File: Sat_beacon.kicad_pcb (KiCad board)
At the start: 4 copper layers, 123.9 x 79.5 mm, 126 parts, among them IC1 LMX2581ESQE_NOPB, IC2 LMX2581ESQE_NOPB, J1 Conn_01x05_Pin, J2 Conn_01x03_Pin, J4 SMA, J5 SMA, J6 Conn_01x04_Pin, Q1 BC817-40, Q2 BC817-40, Q3 BC817-40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

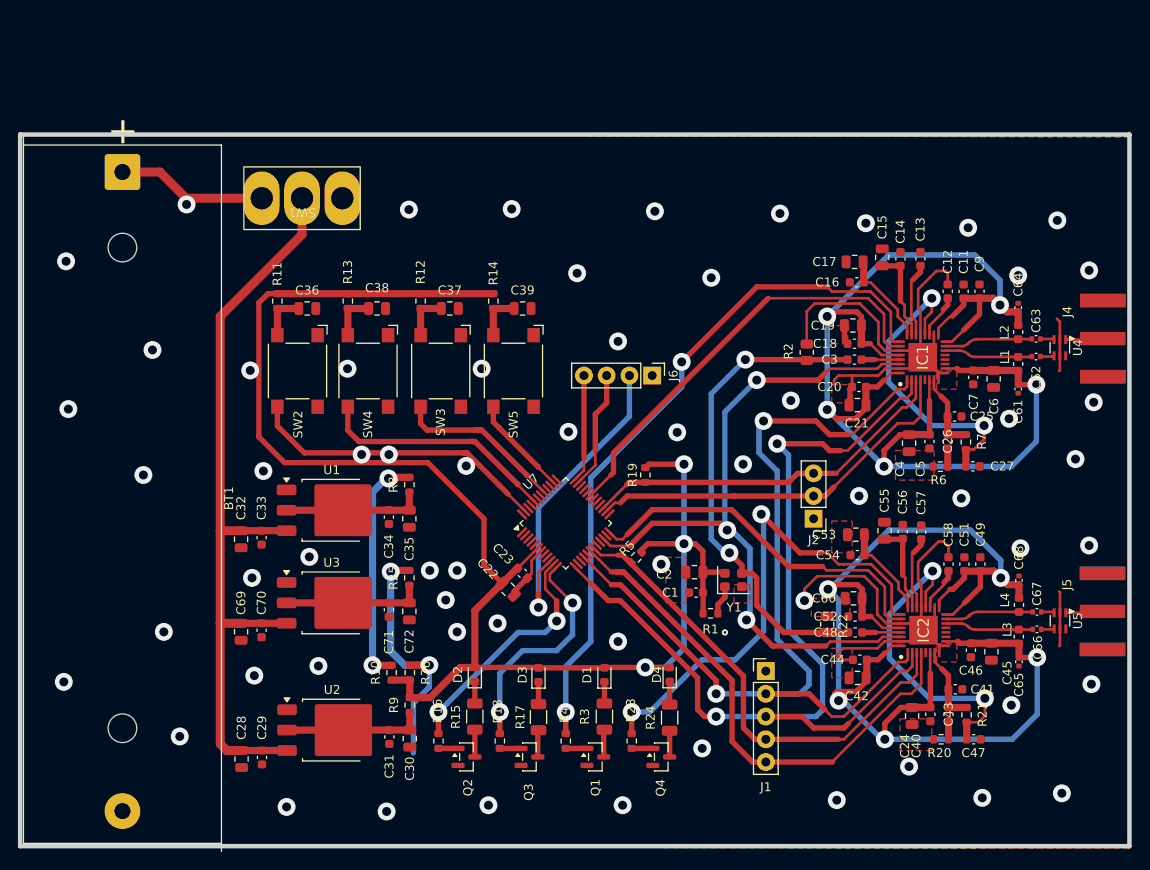
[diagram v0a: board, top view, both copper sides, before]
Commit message: PCB constrains updated for china + added vias, improved vias thanks to improved constrains
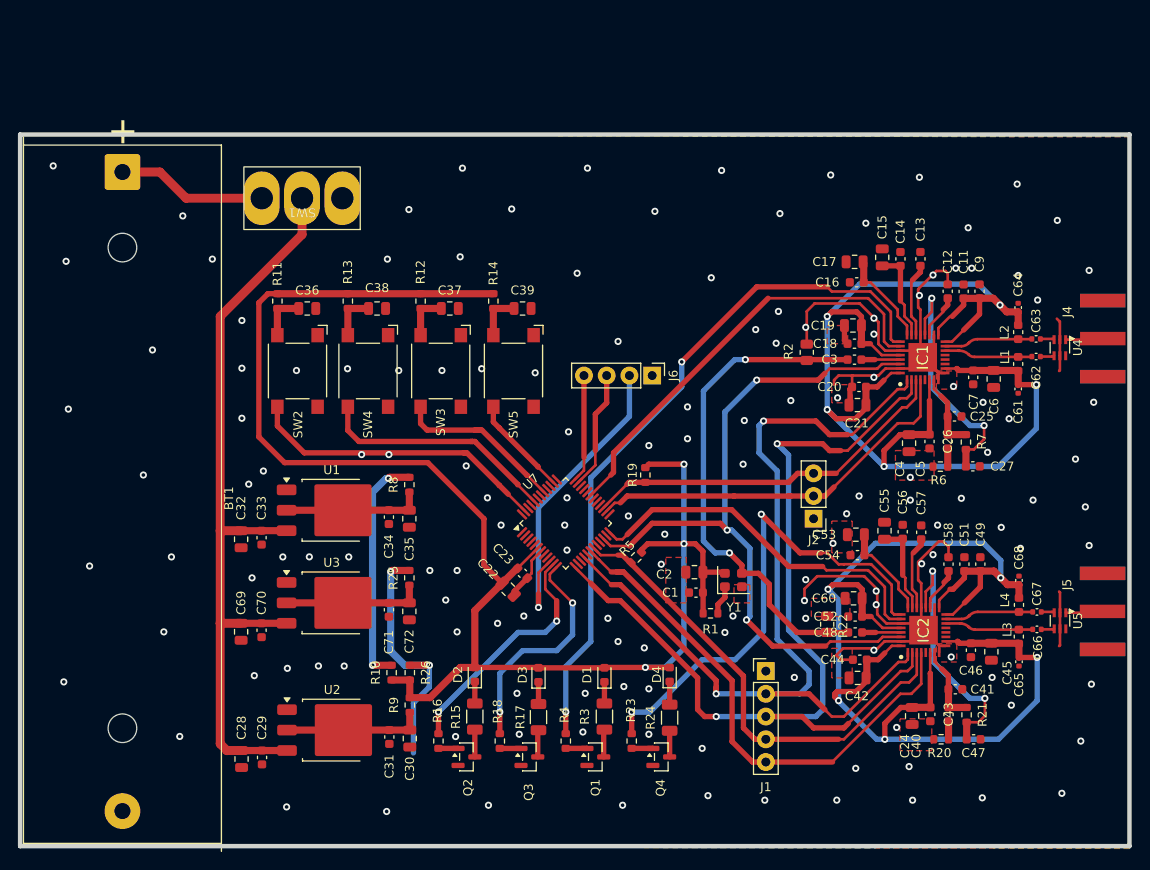
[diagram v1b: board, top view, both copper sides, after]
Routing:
- net /VTUNE_2: track 34.9 -> 28.2 mm
- net /VTUNE_1: track 34.4 -> 28.0 mm
- net VCC_PLL1: track 167.3 -> 162.1 mm, vias 9 -> 7
- net VCC_PLL2: track 169.2 -> 167.1 mm
- net /CLK_10MHZ: track 54.7 -> 56.3 mm
- net GND: vias 58 -> 143
- net /PLL_BTN_1: vias 0 -> 2

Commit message: PCB done and ordered
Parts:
- moved BT1 35.7 mm to (92.2, 50.0), turned to 0 degrees
- moved C69 6.44 mm to (76.3, 108.7), turned to 180 degrees
- moved C32 6.42 mm to (76.3, 98.3), turned to 180 degrees
- moved C28 6.39 mm to (76.3, 122.9), turned to 180 degrees
- moved SW1 4.21 mm to (78.6, 54.6), turned to 90 degrees
- moved J4 1.46 mm to (164.9, 74.4)
- moved J5 1.31 mm to (165.1, 104.9)
- moved C61 1.21 mm to (155.7, 79.9)
- moved C62 1.21 mm to (157.7, 76.3)
- moved C63 1.21 mm to (157.7, 74.3)
- moved L1 1.21 mm to (155.7, 77.1)
- moved L2 1.21 mm to (155.7, 73.6)
- moved U4 1.21 mm to (160.4, 75.3)
- moved U5 1.20 mm to (160.4, 105.7)
- moved C66 1.20 mm to (157.8, 106.7)
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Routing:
- net VCC_PLL2: track 167.1 -> 106.1 mm, vias 9 -> 12
- net VCC_PLL1: track 162.1 -> 112.0 mm, vias 7 -> 12
- net Net-(SW1-B): track 87.4 -> 92.9 mm
- net +BATT: track 16.8 -> 13.6 mm
- net /RF1_DC_N: track 9.97 -> 8.74 mm
- net /RF1_DC_P: track 9.93 -> 8.76 mm
- net /RF2_DC_N: track 9.94 -> 8.92 mm
- net /RF2_DC_P: track 10.0 -> 9.00 mm
- net GND: vias 143 -> 151
- net /PLL_BTN_1: vias 2 -> 0
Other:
- board size 123.9 x 79.5 mm -> 99.1 x 88.1 mm

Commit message: Modifications made while making it run + PLL filter design
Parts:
- C25, C41: value 5n6 -> 3n3
- C26, C43: value 33n -> 56n
- R20, R6: value 560 -> 2k4
